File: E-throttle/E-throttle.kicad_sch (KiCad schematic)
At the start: 66 parts, among them IC1 BTS441TG, J3 Conn_01x11, J4 Conn_01x11, J5 776087-1, J9 Micro_SD_Card, Q1 NMOS, SW1 SW_Push, U1 74HC123, U2 LM317_SOT-223, U3 LM317_SOT-223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

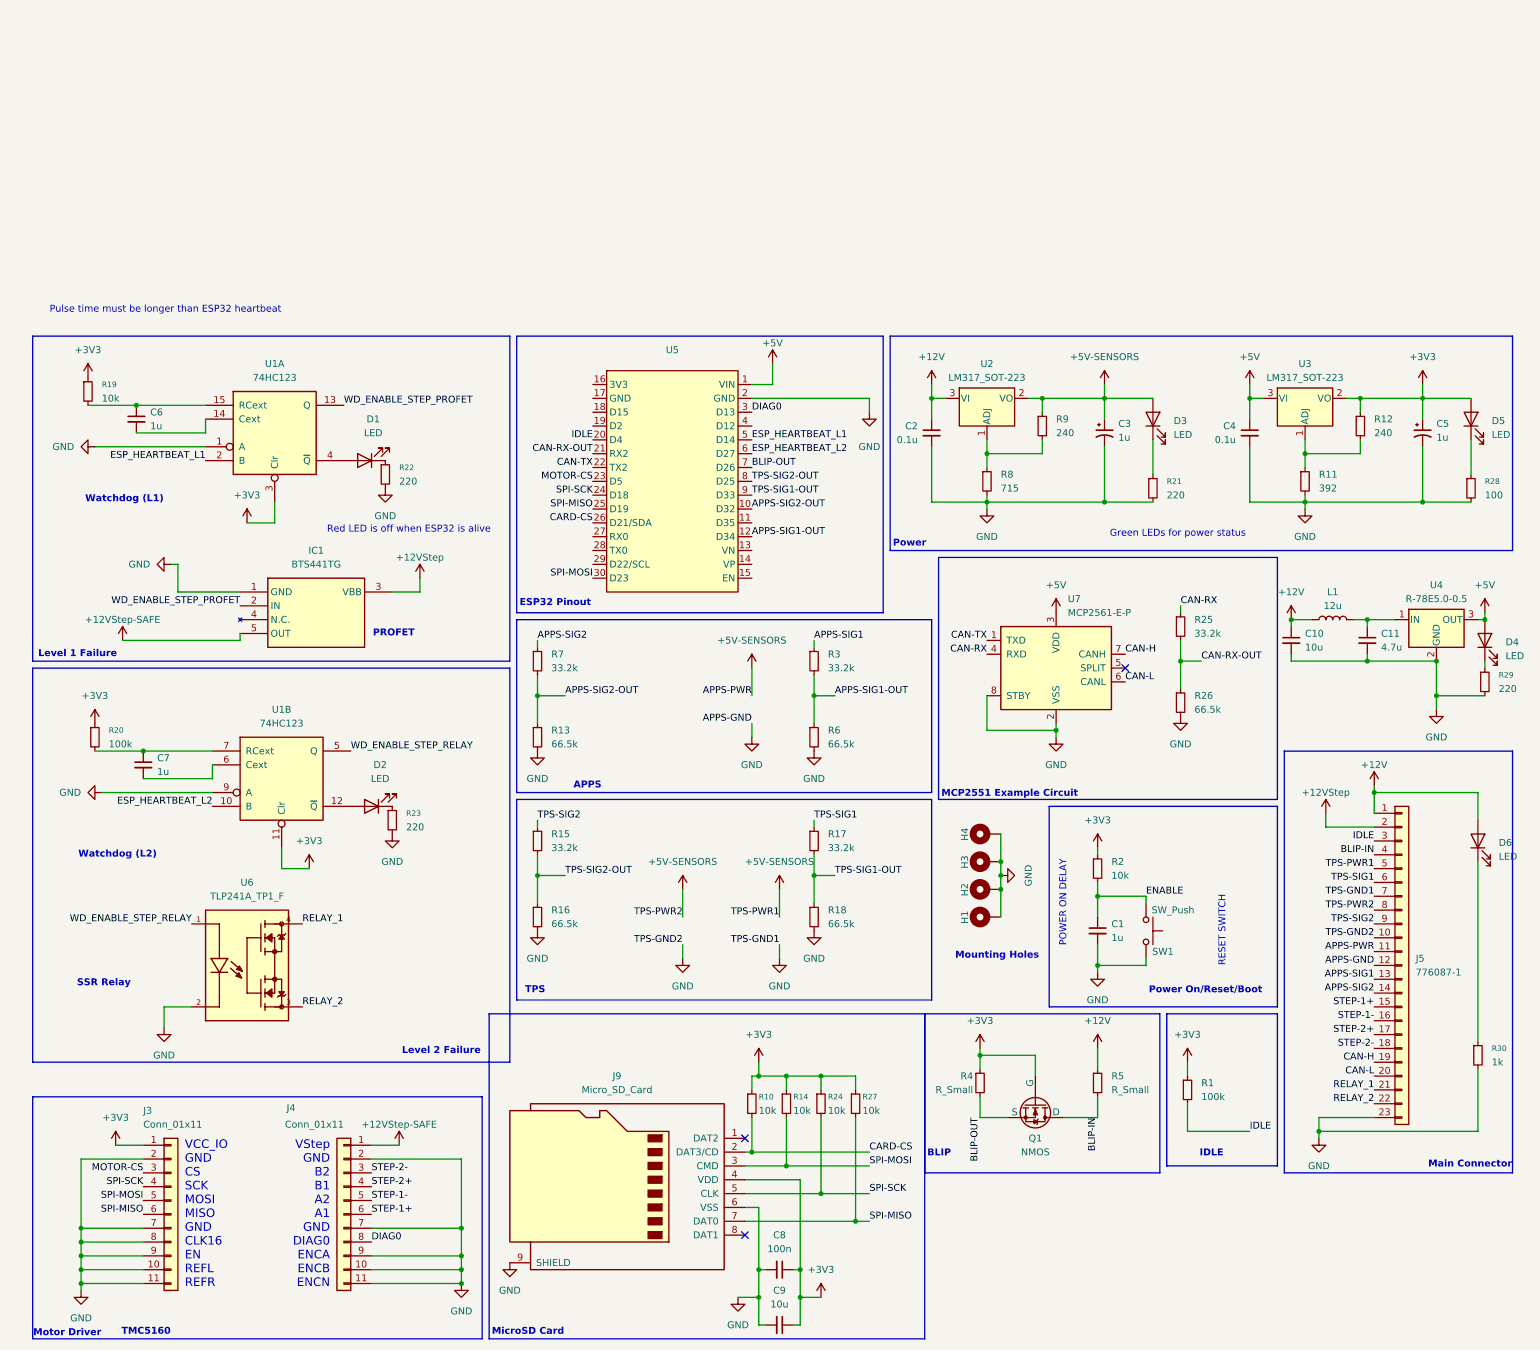
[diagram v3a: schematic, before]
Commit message: arranged components
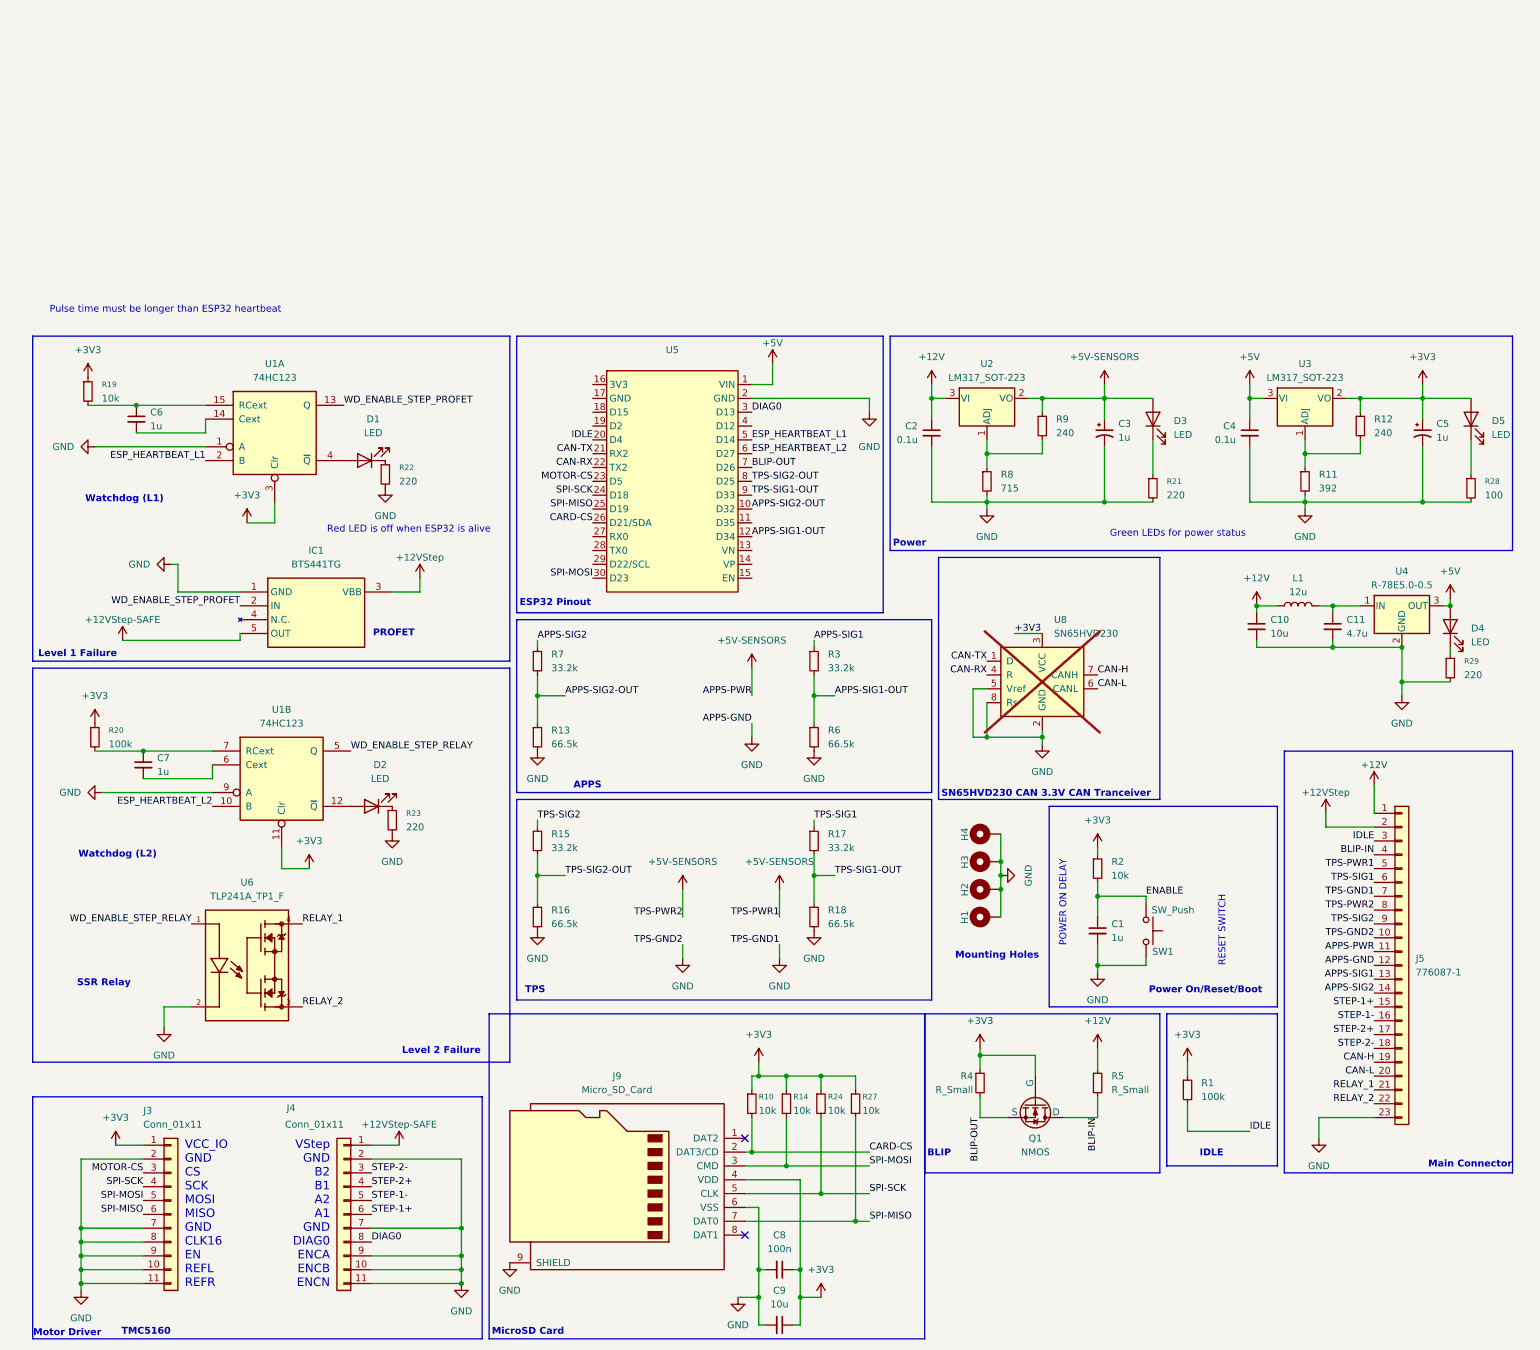
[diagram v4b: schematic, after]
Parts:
- removed D6: LED, symbol Device:LED
- removed R25: 33.2k, Resistor_SMD:R_0805_2012Metric, symbol Device:R_Small
- removed R26: 66.5k, Resistor_SMD:R_0805_2012Metric, symbol Device:R_Small
- removed R30: 1k, symbol Device:R_Small
- removed U7: MCP2561-E-P, Package_DIP:DIP-8_W7.62mm, symbol Interface_CAN_LIN:MCP2561-E-P
- added U8: SN65HVD230, Package_SO:SOIC-8_3.9x4.9mm_P1.27mm, symbol Interface_CAN_LIN:SN65HVD230
- D3, D4, D5: footprint (none) -> LED_SMD:LED_0805_2012Metric_Pad1.15x1.40mm_HandSolder
- R21, R28, R29: footprint (none) -> Resistor_SMD:R_0805_2012Metric
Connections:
- net CAN-RX-OUT is gone; now on net CAN-TX: U5.21 (RX2)
- net +3V3: now also U8.3 (VCC)
- net CAN-H: now also U8.7 (CANH)
- net CAN-L: now also U8.6 (CANL)
- net CAN-RX: now also U5.22 (TX2), U8.4 (R)
- net CAN-TX: now also U8.1 (D); no longer U5.22 (TX2)
- net GND: now also U8.2 (GND), U8.5 (Vref), U8.8 (Rs)
- no-connect marks 3 -> 2
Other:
- note added: "SN65HVD230 CAN 3.3V CAN Tranceiver"
- note removed: "MCP2551 Example Circuit"
- moved on the sheet: C10, C11, D4, L1, R29, U4

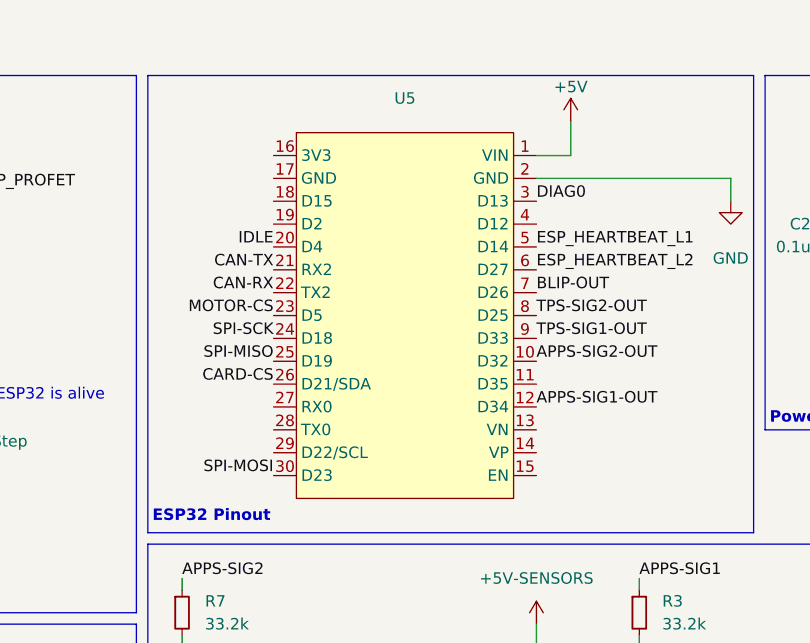
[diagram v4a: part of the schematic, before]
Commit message: Added majority of routing to PCB layout
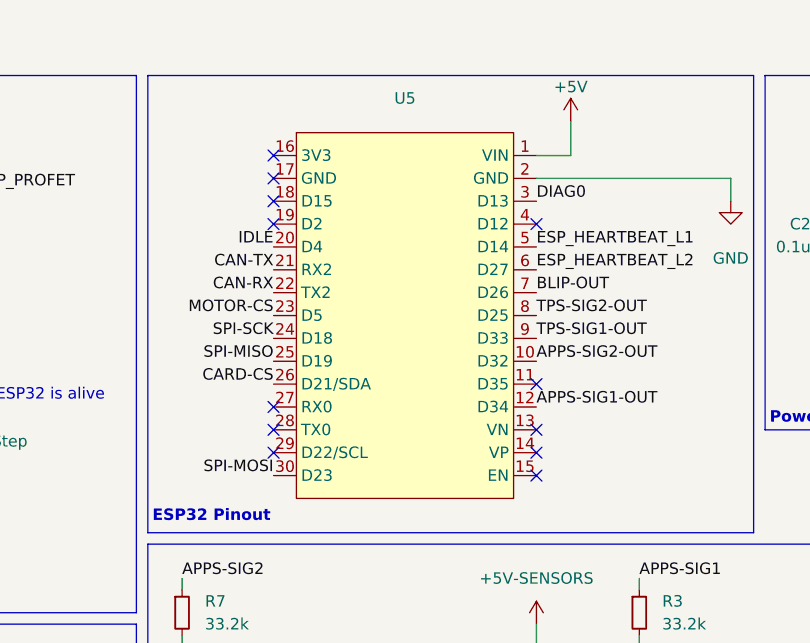
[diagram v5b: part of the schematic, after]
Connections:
- no-connect marks 2 -> 14

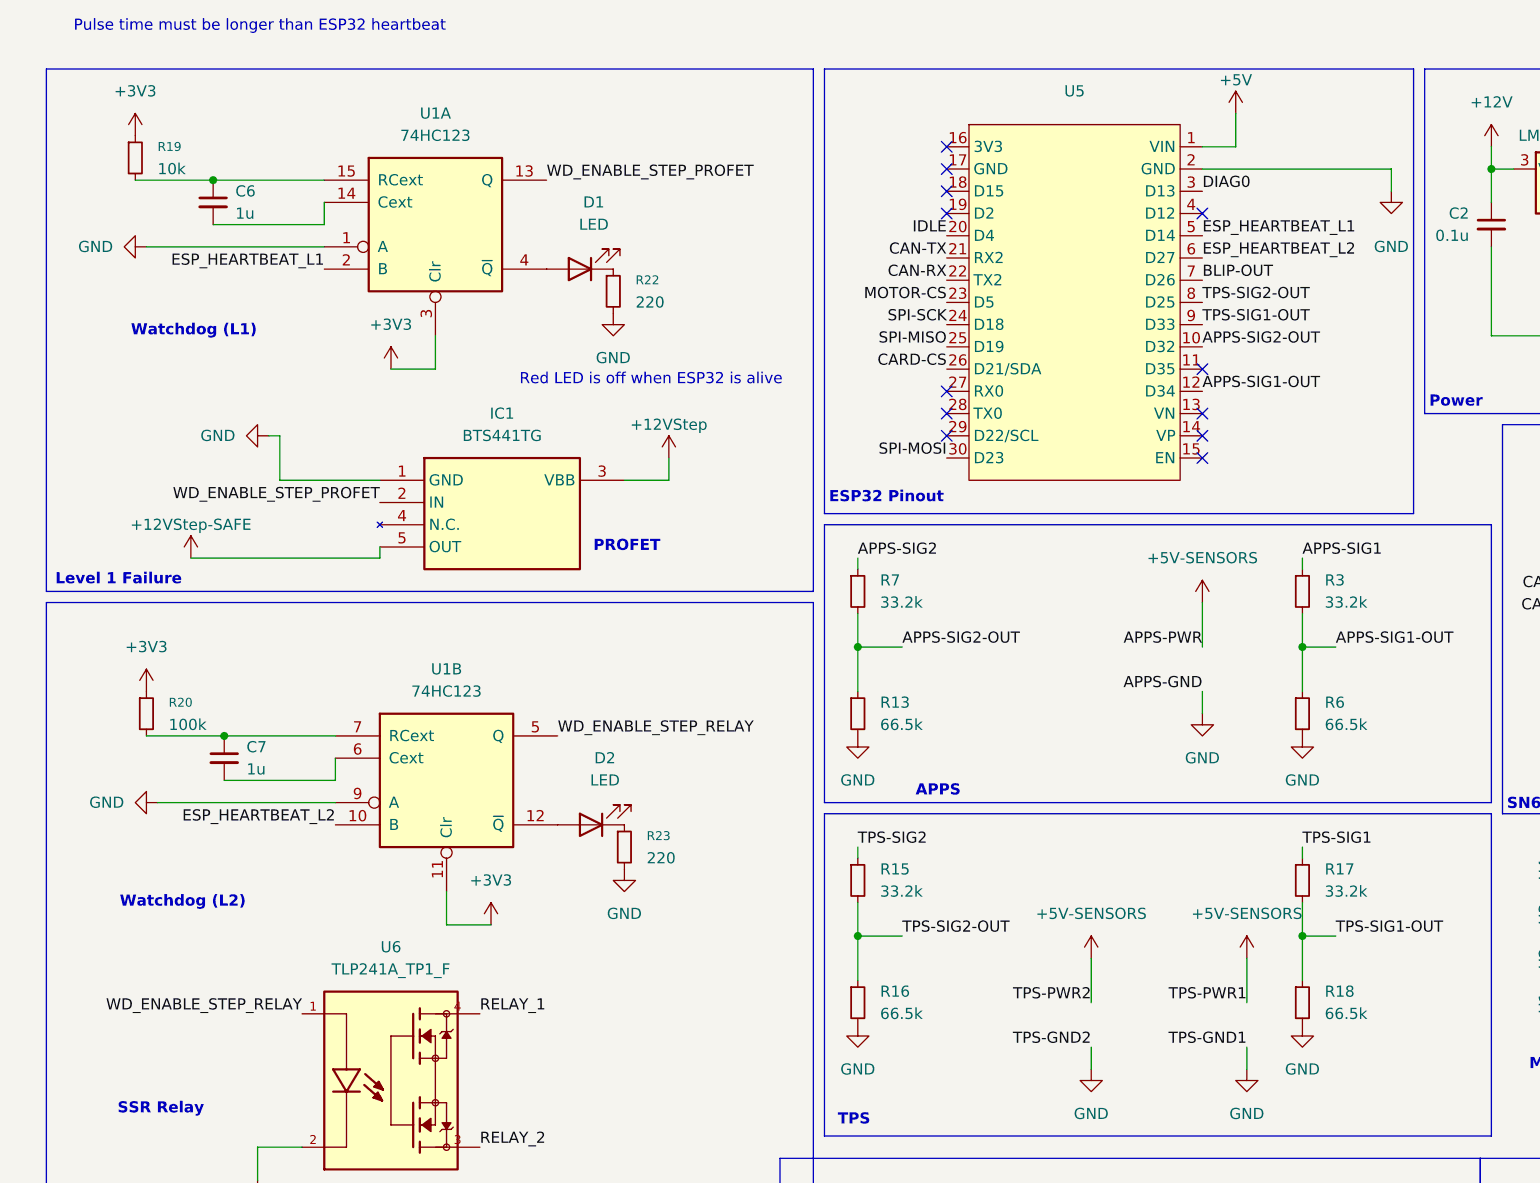
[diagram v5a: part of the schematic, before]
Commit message: added vias, ran DRC
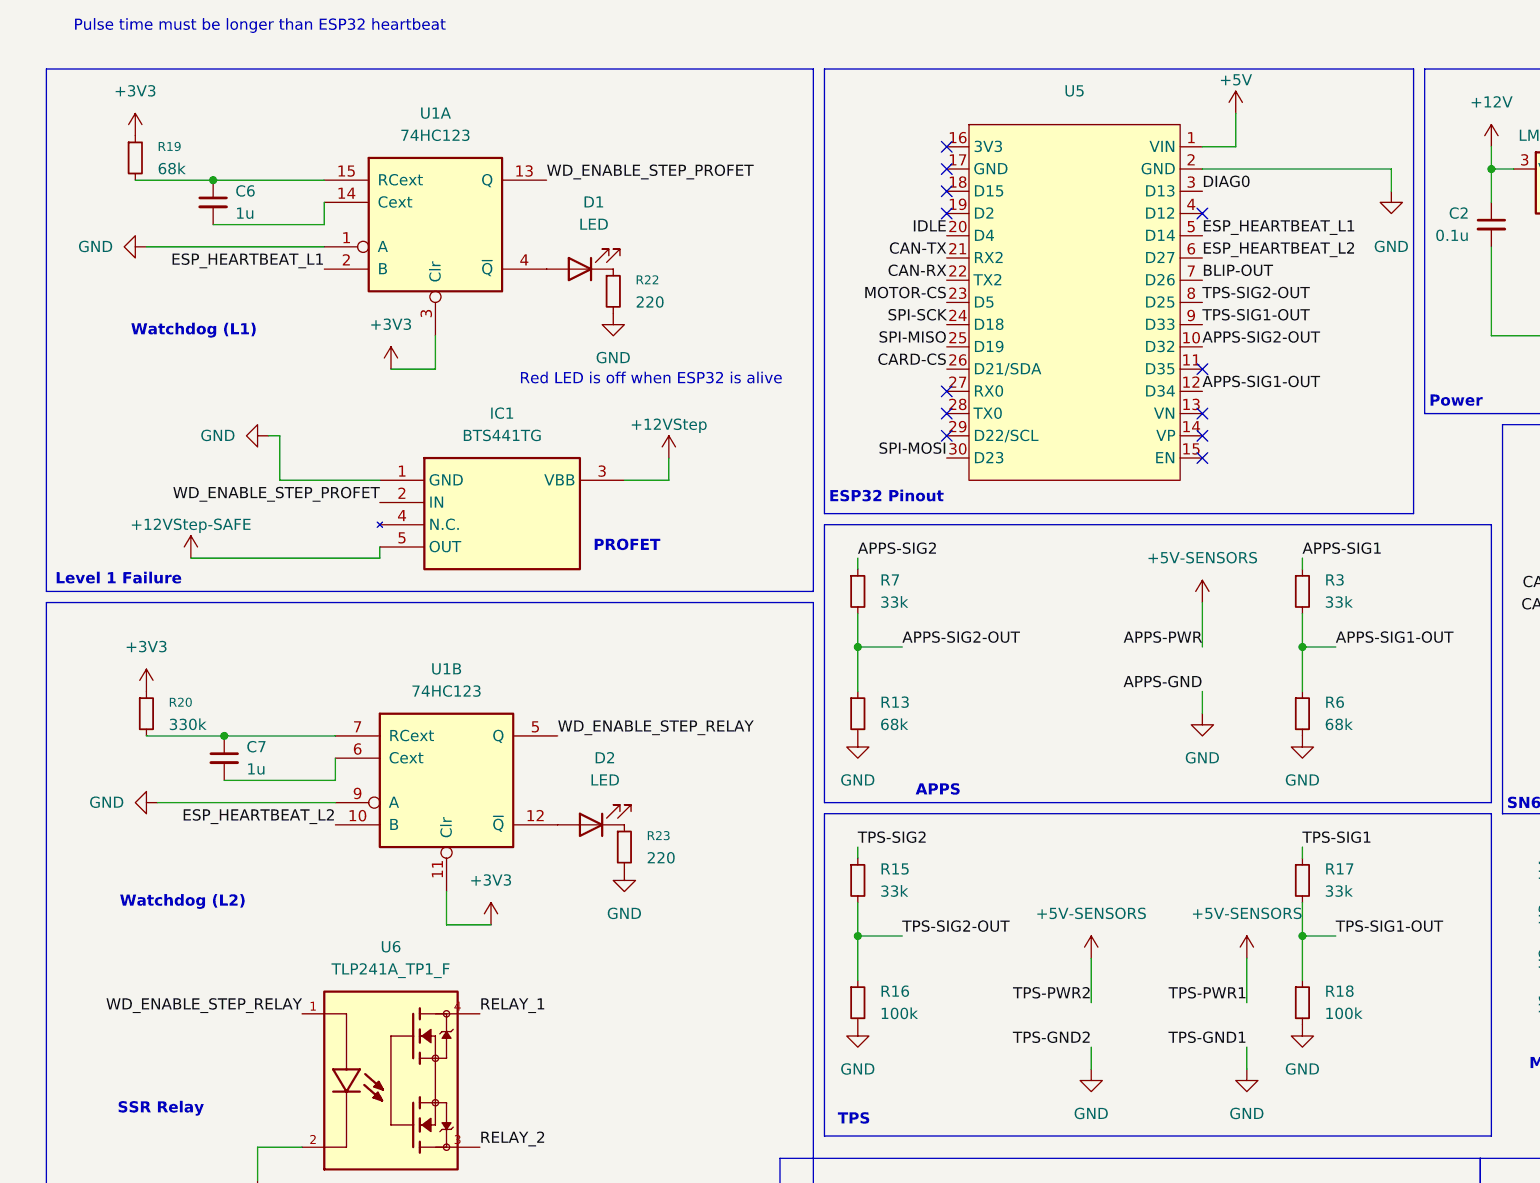
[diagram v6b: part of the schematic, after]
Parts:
- R13, R6: value 66.5k -> 68k
- R15, R17, R3, R7: value 33.2k -> 33k
- R16, R18: value 66.5k -> 100k
- R19: value 10k -> 68k
- R20: value 100k -> 330k

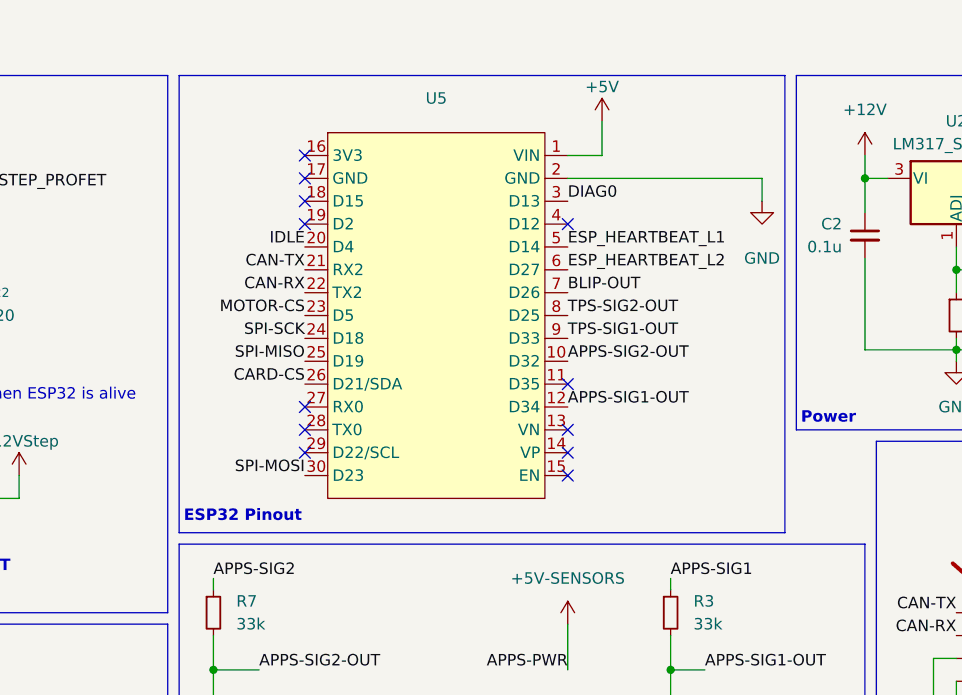
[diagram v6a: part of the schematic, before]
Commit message: Added THT filtering capacitors
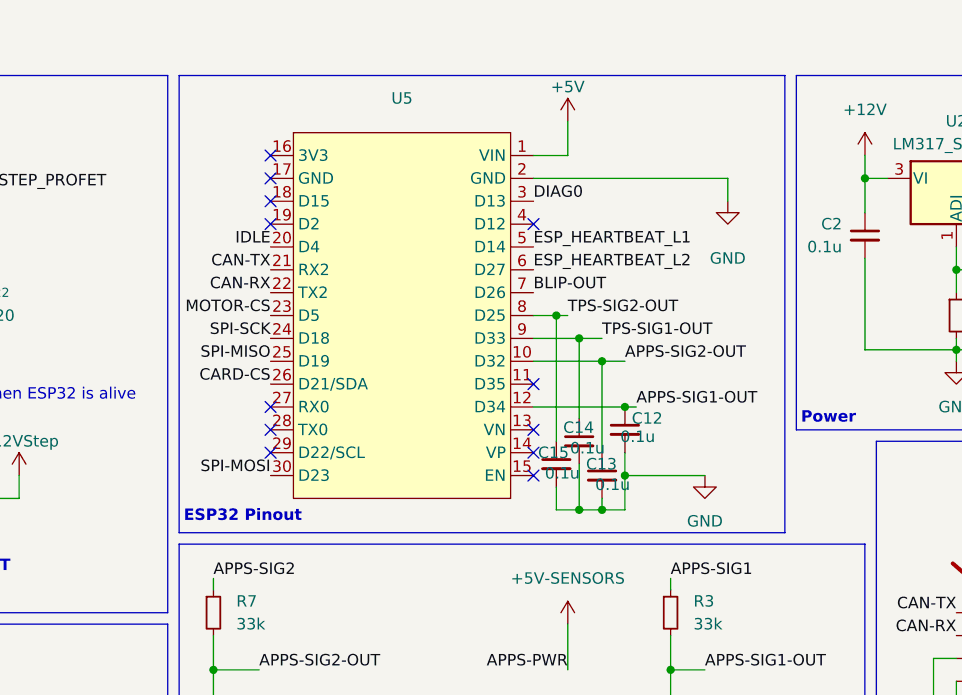
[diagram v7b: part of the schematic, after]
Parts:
- added C12, C13, C14, C15: 0.1u, Capacitor_THT:C_Radial_D4.0mm_H7.0mm_P1.50mm, symbol Device:C_Small
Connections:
- net APPS-SIG1-OUT: now also C12.1
- net APPS-SIG2-OUT: now also C13.1
- net GND: now also C12.2, C13.2, C14.2, C15.2
- net TPS-SIG1-OUT: now also C14.1
- net TPS-SIG2-OUT: now also C15.1
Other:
- moved on the sheet: U5
